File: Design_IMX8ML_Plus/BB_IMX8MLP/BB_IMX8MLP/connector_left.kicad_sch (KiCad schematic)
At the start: 8 parts, among them J3 Front_Left, J4 Back_Left

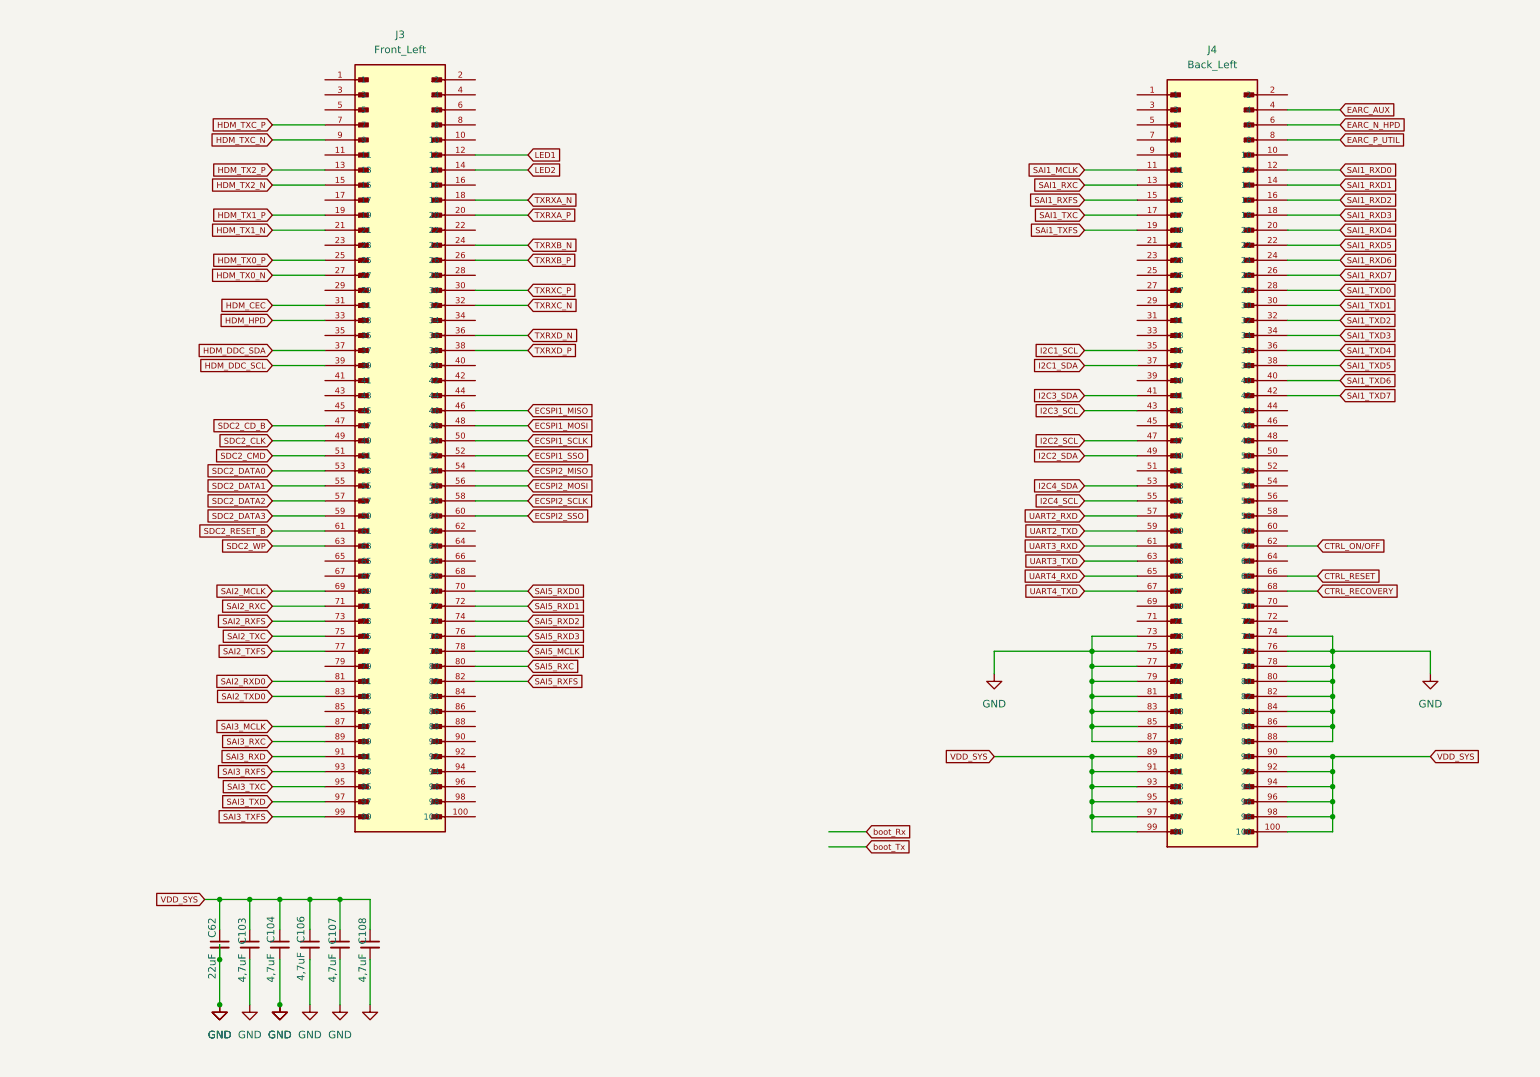
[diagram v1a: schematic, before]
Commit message: [CPU/BB] Improving the conection between the cpu and BB
* Reorganization of the components in the Base board.
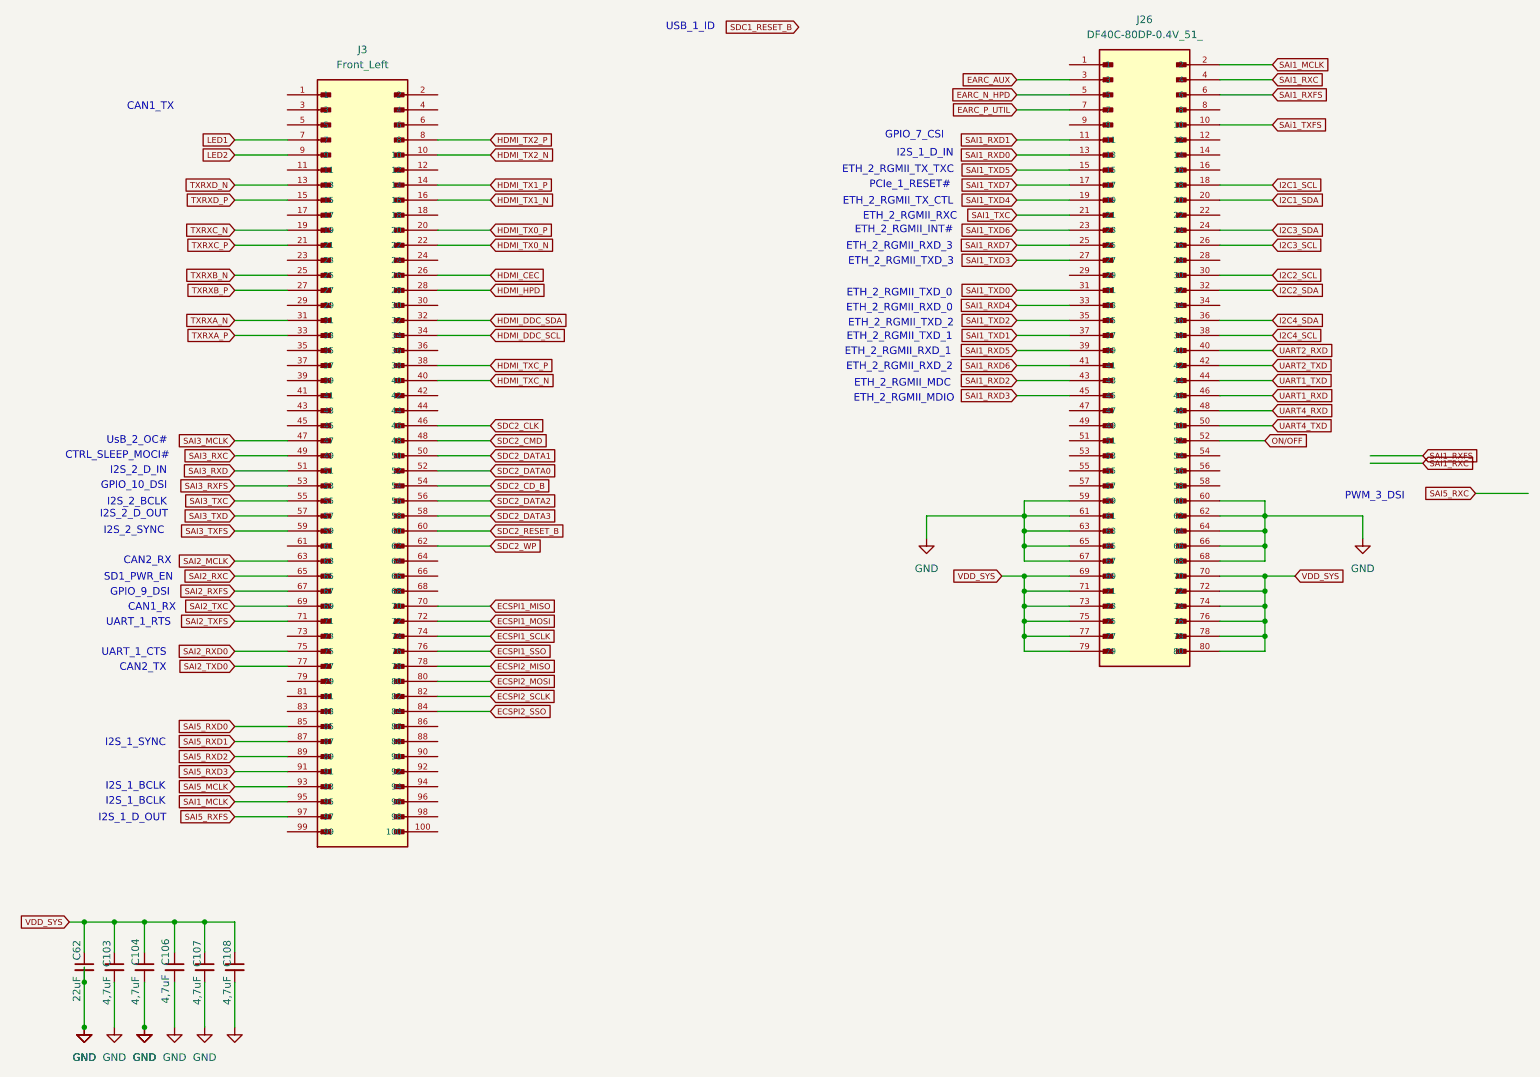
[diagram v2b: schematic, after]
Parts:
- removed J4: Back_Left, _W_SBC:HIROSE_DF40C-100DS-0.4V_51_, symbol CONN_DF40C-100DS-0_4V51_HIR:DF40C-100DP-0.4V_51_
- added J26: DF40C-80DP-0.4V_51_, _W_SBC:HRS_DF40C-80DP-0.4V_51_, symbol DF40C-80DP-0.4V_51_:DF40C-80DP-0.4V_51_
- J3: footprint _W_SBC:HIROSE_DF40C-100DS-0.4V_51_ -> _W_SBC:HRS_DF40C-100DP-0.4V_51_
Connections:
- net HDM_CEC is gone; now on net TXRXA_N: J3.31
- net HDM_HPD is gone; now on net TXRXA_P: J3.33
- net HDM_TX0_N is gone; now on net TXRXB_P: J3.27
- net HDM_TX0_P is gone; now on net TXRXB_N: J3.25
- net HDM_TX1_N is gone; now on net TXRXC_P: J3.21
- net HDM_TX1_P is gone; now on net TXRXC_N: J3.19
- net HDM_TX2_N is gone; now on net TXRXD_P: J3.15
- net HDM_TX2_P is gone; now on net TXRXD_N: J3.13
- net HDM_TXC_N is gone; now on net LED2: J3.9
- net HDM_TXC_P is gone; now on net LED1: J3.7
- net EARC_AUX: now also J26.3
- net EARC_N_HPD: now also J26.5
- net EARC_P_UTIL: now also J26.7
- net ECSPI1_MISO: now also J3.70; no longer J3.46
- net ECSPI1_MOSI: now also J3.72; no longer J3.48
- net ECSPI1_SCLK: now also J3.74; no longer J3.50
- net ECSPI1_SSO: now also J3.76; no longer J3.52
- net ECSPI2_MISO: now also J3.78; no longer J3.54
- net ECSPI2_MOSI: now also J3.80; no longer J3.56
- net ECSPI2_SCLK: now also J3.82; no longer J3.58
- net ECSPI2_SSO: now also J3.84; no longer J3.60
- net GND: now also J26.59, J26.60, J26.61, J26.62, J26.63, J26.64, J26.65, J26.66, J26.67, J26.68
- net I2C1_SCL: now also J26.18
- net I2C1_SDA: now also J26.20
- net I2C2_SCL: now also J26.30
- net I2C2_SDA: now also J26.32
- net I2C3_SCL: now also J26.26
- net I2C3_SDA: now also J26.24
- net I2C4_SCL: now also J26.38
- net I2C4_SDA: now also J26.36
- net LED1: no longer J3.12
- net LED2: no longer J3.14
- net SAI1_MCLK: now also J3.95, J26.2
- net SAI1_RXC: now also J26.4
- net SAI1_RXD0: now also J26.13
- net SAI1_RXD1: now also J26.11
- net SAI1_RXD2: now also J26.43
- net SAI1_RXD3: now also J26.45
- net SAI1_RXD4: now also J26.33
- net SAI1_RXD5: now also J26.39
- net SAI1_RXD6: now also J26.41
- net SAI1_RXD7: now also J26.25
- net SAI1_RXFS: now also J26.6
- net SAI1_TXC: now also J26.21
- net SAI1_TXD0: now also J26.31
- net SAI1_TXD1: now also J26.37
- net SAI1_TXD2: now also J26.35
- net SAI1_TXD3: now also J26.27
- net SAI1_TXD4: now also J26.19
- net SAI1_TXD5: now also J26.15
- net SAI1_TXD6: now also J26.23
- net SAI1_TXD7: now also J26.17
- net SAI2_MCLK: now also J3.63; no longer J3.69
- net SAI2_RXC: now also J3.65; no longer J3.71
- net SAI2_RXD0: now also J3.75; no longer J3.81
- net SAI2_RXFS: now also J3.67; no longer J3.73
- net SAI2_TXC: now also J3.69; no longer J3.75
- net SAI2_TXD0: now also J3.77; no longer J3.83
- net SAI2_TXFS: now also J3.71; no longer J3.77
- net SAI3_MCLK: now also J3.47; no longer J3.87
- net SAI3_RXC: now also J3.49; no longer J3.89
- net SAI3_RXD: now also J3.51; no longer J3.91
- net SAI3_RXFS: now also J3.53; no longer J3.93
- net SAI3_TXC: now also J3.55; no longer J3.95
- net SAI3_TXD: now also J3.57; no longer J3.97
- net SAI3_TXFS: now also J3.59; no longer J3.99
- net SAI5_MCLK: now also J3.93; no longer J3.78
- net SAI5_RXC: no longer J3.80
- net SAI5_RXD0: now also J3.85; no longer J3.70
- net SAI5_RXD1: now also J3.87; no longer J3.72
- net SAI5_RXD2: now also J3.89; no longer J3.74
- net SAI5_RXD3: now also J3.91; no longer J3.76
- net SAI5_RXFS: now also J3.97; no longer J3.82
- net SAi1_TXFS: now also J26.10
- net SDC2_CD_B: now also J3.54; no longer J3.47
- net SDC2_CLK: now also J3.46; no longer J3.49
- net SDC2_CMD: now also J3.48; no longer J3.51
- net SDC2_DATA0: now also J3.52; no longer J3.53
- net SDC2_DATA1: now also J3.50; no longer J3.55
- net SDC2_DATA2: now also J3.56; no longer J3.57
- net SDC2_DATA3: now also J3.58; no longer J3.59
- net SDC2_RESET_B: now also J3.60; no longer J3.61
- net SDC2_WP: now also J3.62; no longer J3.63
- net TXRXA_N: no longer J3.18
- net TXRXA_P: no longer J3.20
- net TXRXB_N: no longer J3.24
- net TXRXB_P: no longer J3.26
- net TXRXC_N: no longer J3.32
- net TXRXC_P: no longer J3.30
- net TXRXD_N: no longer J3.36
- net TXRXD_P: no longer J3.38
- net UART2_RXD: now also J26.40
- net UART2_TXD: now also J26.42
- net UART4_RXD: now also J26.48
- net UART4_TXD: now also J26.50
- net VDD_SYS: now also J26.69, J26.70, J26.71, J26.72, J26.73, J26.74, J26.75, J26.76, J26.77, J26.78, J26.79, J26.80
- net HDMI_TX2_N: now reaches J3.10
- net HDMI_TX1_N: now reaches J3.16
- net HDMI_TX0_N: now reaches J3.22
- net HDMI_HPD: now reaches J3.28
- net HDMI_DDC_SCL: now reaches J3.34
- net HDMI_TXC_N: now reaches J3.40
- net HDMI_TX2_P: now reaches J3.8
- net HDM_DDC_SCL: no longer names the net of J3.39
- net HDM_DDC_SDA: no longer names the net of J3.37
- new net HDMI_CEC: J3.26
- new net HDMI_DDC_SDA: J3.32
- new net HDMI_TX0_P: J3.20
- new net HDMI_TX1_P: J3.14
- new net HDMI_TXC_P: J3.38
- new net ON/OFF: J26.52
- new net UART1_RXD: J26.46
- new net UART1_TXD: J26.44
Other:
- note added: "CAN1_RX"
- note added: "CAN1_TX"
- note added: "CAN2_RX"
- note added: "CAN2_TX"
- note added: "CTRL_SLEEP_MOCI#"
- note added: "ETH_2_RGMII_INT#"
- note added: "ETH_2_RGMII_MDC"
- note added: "ETH_2_RGMII_MDIO"
- note added: "ETH_2_RGMII_RXC"
- note added: "ETH_2_RGMII_RXD_0"
- note added: "ETH_2_RGMII_RXD_1"
- note added: "ETH_2_RGMII_RXD_2"
- note added: "ETH_2_RGMII_RXD_3"
- note added: "ETH_2_RGMII_TXD_0"
- note added: "ETH_2_RGMII_TXD_1"
- note added: "ETH_2_RGMII_TXD_2"
- note added: "ETH_2_RGMII_TXD_3"
- note added: "ETH_2_RGMII_TX_CTL"
- note added: "ETH_2_RGMII_TX_TXC"
- note added: "GPIO_10_DSI"
- note added: "GPIO_7_CSI"
- note added: "GPIO_9_DSI"
- note added: "I2S_1_BCLK"
- note added: "I2S_1_D_IN"
- note added: "I2S_1_D_OUT"
- note added: "I2S_1_SYNC"
- note added: "I2S_2_BCLK"
- note added: "I2S_2_D_IN"
- note added: "I2S_2_D_OUT"
- note added: "I2S_2_SYNC"
- note added: "PCIe_1_RESET#"
- note added: "PWM_3_DSI"
- note added: "SD1_PWR_EN"
- note added: "UART_1_CTS"
- note added: "UART_1_RTS"
- note added: "USB_1_ID"
- note added: "UsB_2_OC#"
- moved on the sheet: C103, C104, C106, C107, C108, C62, J3

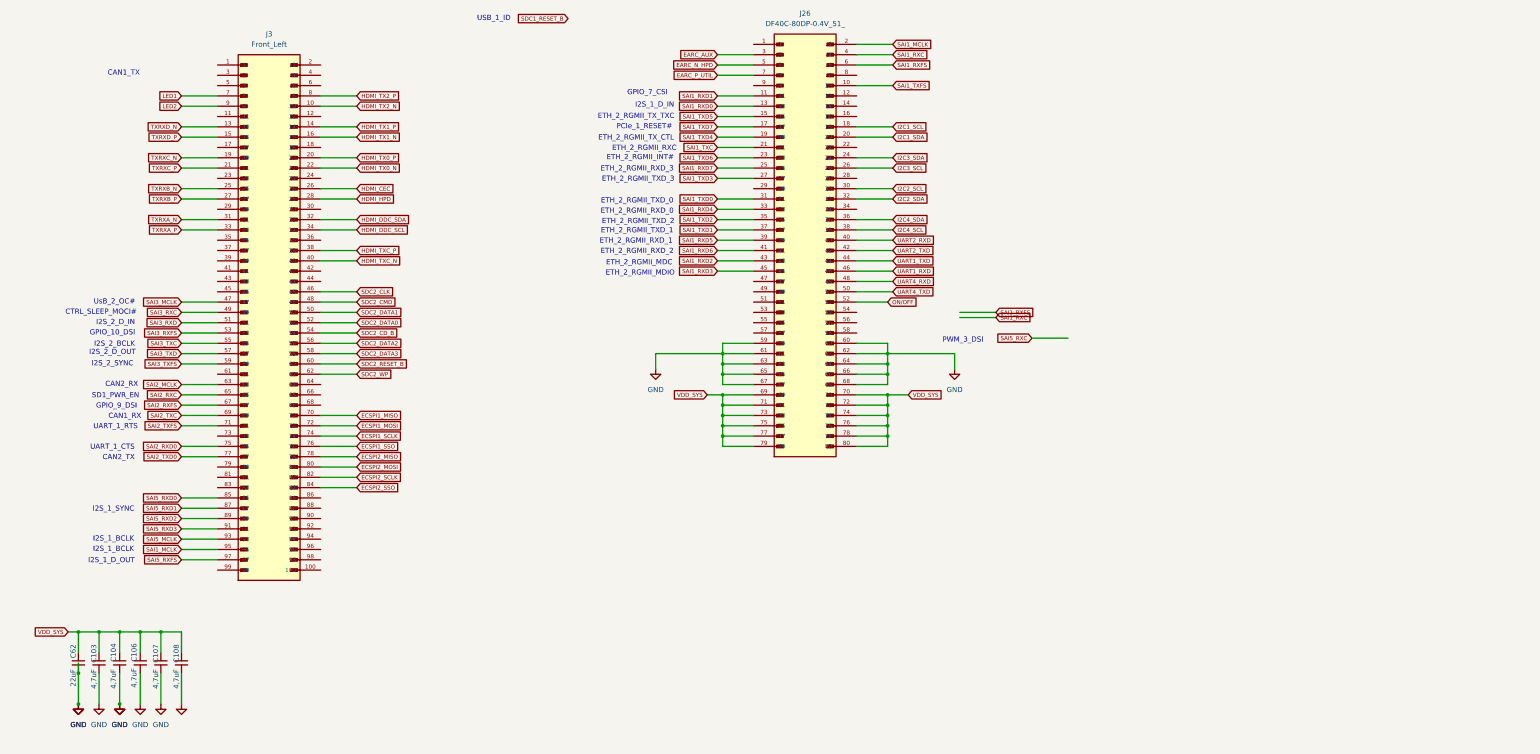
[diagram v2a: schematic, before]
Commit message: [BB_IMX8MLP IMX8MLP] Actuallizated to 9.0 kicad version
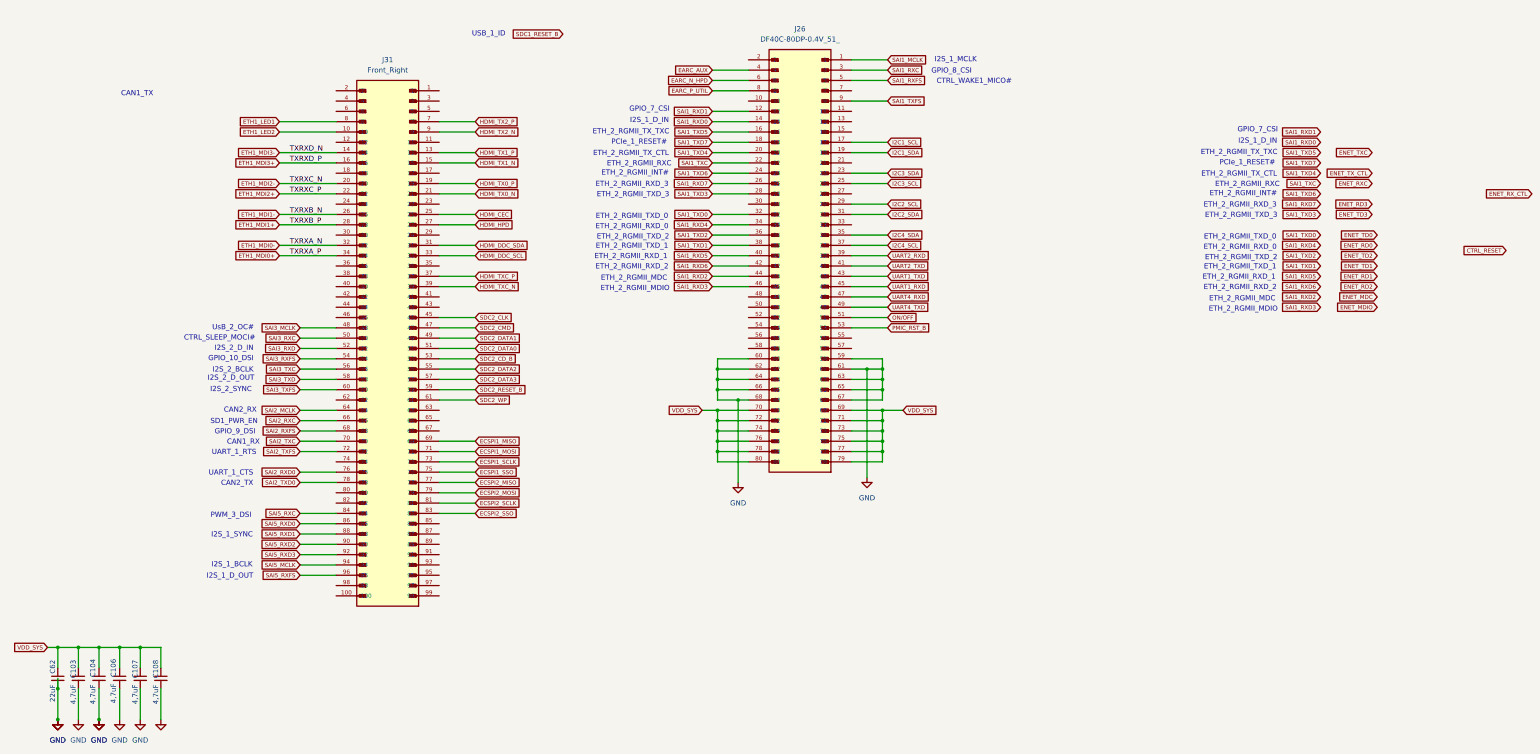
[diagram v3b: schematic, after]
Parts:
- removed J3: Front_Left, _W_SBC:HRS_DF40C-100DP-0.4V_51_, symbol CONN_DF40C-100DS-0_4V51_HIR:DF40C-100DP-0.4V_51_
- added J31: Front_Right, _W_SBC:HRS_DF40C-100DP-0.4V_51_, symbol CONN_DF40C-100DS-0_4V51_HIR:DF40C-100DP-0.4V_51_
- J26: Price None -> 2
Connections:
- net EARC_AUX: now also J26.4; no longer J26.3
- net EARC_N_HPD: now also J26.6; no longer J26.5
- net EARC_P_UTIL: now also J26.8; no longer J26.7
- net ECSPI1_MISO: now also J31.69
- net ECSPI1_MOSI: now also J31.71
- net ECSPI1_SCLK: now also J31.73
- net ECSPI1_SSO: now also J31.75
- net ECSPI2_MISO: now also J31.77
- net ECSPI2_MOSI: now also J31.79
- net ECSPI2_SCLK: now also J31.81
- net ECSPI2_SSO: now also J31.83
- net HDMI_CEC: now also J31.25
- net HDMI_DDC_SCL: now also J31.33
- net HDMI_DDC_SDA: now also J31.31
- net HDMI_HPD: now also J31.27
- net HDMI_TX0_N: now also J31.21
- net HDMI_TX0_P: now also J31.19
- net HDMI_TX1_N: now also J31.15
- net HDMI_TX1_P: now also J31.13
- net HDMI_TX2_N: now also J31.9
- net HDMI_TX2_P: now also J31.7
- net HDMI_TXC_N: now also J31.39
- net HDMI_TXC_P: now also J31.37
- net I2C1_SCL: now also J26.17; no longer J26.18
- net I2C1_SDA: now also J26.19; no longer J26.20
- net I2C2_SCL: now also J26.29; no longer J26.30
- net I2C2_SDA: now also J26.31; no longer J26.32
- net I2C3_SCL: now also J26.25; no longer J26.26
- net I2C3_SDA: now also J26.23; no longer J26.24
- net I2C4_SCL: now also J26.37; no longer J26.38
- net I2C4_SDA: now also J26.35; no longer J26.36
- net ON/OFF: now also J26.51; no longer J26.52
- net SAI1_MCLK: now also J26.1; no longer J26.2
- net SAI1_RXC: now also J26.3; no longer J26.4
- net SAI1_RXD0: now also J26.14; no longer J26.13
- net SAI1_RXD1: now also J26.12; no longer J26.11
- net SAI1_RXD2: now also J26.44; no longer J26.43
- net SAI1_RXD3: now also J26.46; no longer J26.45
- net SAI1_RXD4: now also J26.34; no longer J26.33
- net SAI1_RXD5: now also J26.40; no longer J26.39
- net SAI1_RXD6: now also J26.42; no longer J26.41
- net SAI1_RXD7: now also J26.26; no longer J26.25
- net SAI1_RXFS: now also J26.5; no longer J26.6
- net SAI1_TXC: now also J26.22; no longer J26.21
- net SAI1_TXD0: now also J26.32; no longer J26.31
- net SAI1_TXD1: now also J26.38; no longer J26.37
- net SAI1_TXD2: now also J26.36; no longer J26.35
- net SAI1_TXD3: now also J26.28; no longer J26.27
- net SAI1_TXD4: now also J26.20; no longer J26.19
- net SAI1_TXD5: now also J26.16; no longer J26.15
- net SAI1_TXD6: now also J26.24; no longer J26.23
- net SAI1_TXD7: now also J26.18; no longer J26.17
- net SAI2_MCLK: now also J31.64
- net SAI2_RXC: now also J31.66
- net SAI2_RXD0: now also J31.76
- net SAI2_RXFS: now also J31.68
- net SAI2_TXC: now also J31.70
- net SAI2_TXD0: now also J31.78
- net SAI2_TXFS: now also J31.72
- net SAI3_MCLK: now also J31.48
- net SAI3_RXC: now also J31.50
- net SAI3_RXD: now also J31.52
- net SAI3_RXFS: now also J31.54
- net SAI3_TXC: now also J31.56
- net SAI3_TXD: now also J31.58
- net SAI3_TXFS: now also J31.60
- net SAI5_MCLK: now also J31.94
- net SAI5_RXC: now also J31.84
- net SAI5_RXD0: now also J31.86
- net SAI5_RXD1: now also J31.88
- net SAI5_RXD2: now also J31.90
- net SAI5_RXD3: now also J31.92
- net SAI5_RXFS: now also J31.96
- net SDC2_CD_B: now also J31.53
- net SDC2_CLK: now also J31.45
- net SDC2_CMD: now also J31.47
- net SDC2_DATA0: now also J31.51
- net SDC2_DATA1: now also J31.49
- net SDC2_DATA2: now also J31.55
- net SDC2_DATA3: now also J31.57
- net SDC2_RESET_B: now also J31.59
- net SDC2_WP: now also J31.61
- net UART1_RXD: now also J26.45; no longer J26.46
- net UART1_TXD: now also J26.43; no longer J26.44
- net UART2_RXD: now also J26.39; no longer J26.40
- net UART2_TXD: now also J26.41; no longer J26.42
- net UART4_RXD: now also J26.47; no longer J26.48
- net UART4_TXD: now also J26.49; no longer J26.50
- net PMIC_RST_B: now reaches J26.53
- net SAI1_TXFS: now reaches J26.9
- net SAi1_TXFS: no longer names the net of J26.10
- new net ETH1_LED1: J31.8
- new net ETH1_LED2: J31.10
- new net ETH1_MDI0+: J31.34
- new net ETH1_MDI0-: J31.32
- new net ETH1_MDI1+: J31.28
- new net ETH1_MDI1-: J31.26
- new net ETH1_MDI2+: J31.22
- new net ETH1_MDI2-: J31.20
- new net ETH1_MDI3+: J31.16
- new net ETH1_MDI3-: J31.14
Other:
- note added: "CTRL_WAKE1_MICO#"
- note added: "GPIO_8_CSI"
- note added: "I2S_1_MCLK"
- moved on the sheet: C103, C104, C106, C107, C108, C62
